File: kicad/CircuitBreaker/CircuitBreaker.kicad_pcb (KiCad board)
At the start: 2 copper layers, 71.6 x 27.5 mm, 59 parts, among them J1 PH2.54, J4 PH2.54, J5 downlink, J6 uplink, J7 PWN-In-5v, SW1 usbIAP, T1 CT104D, T2 CT104D, T3 CT104D, T4 CT104D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

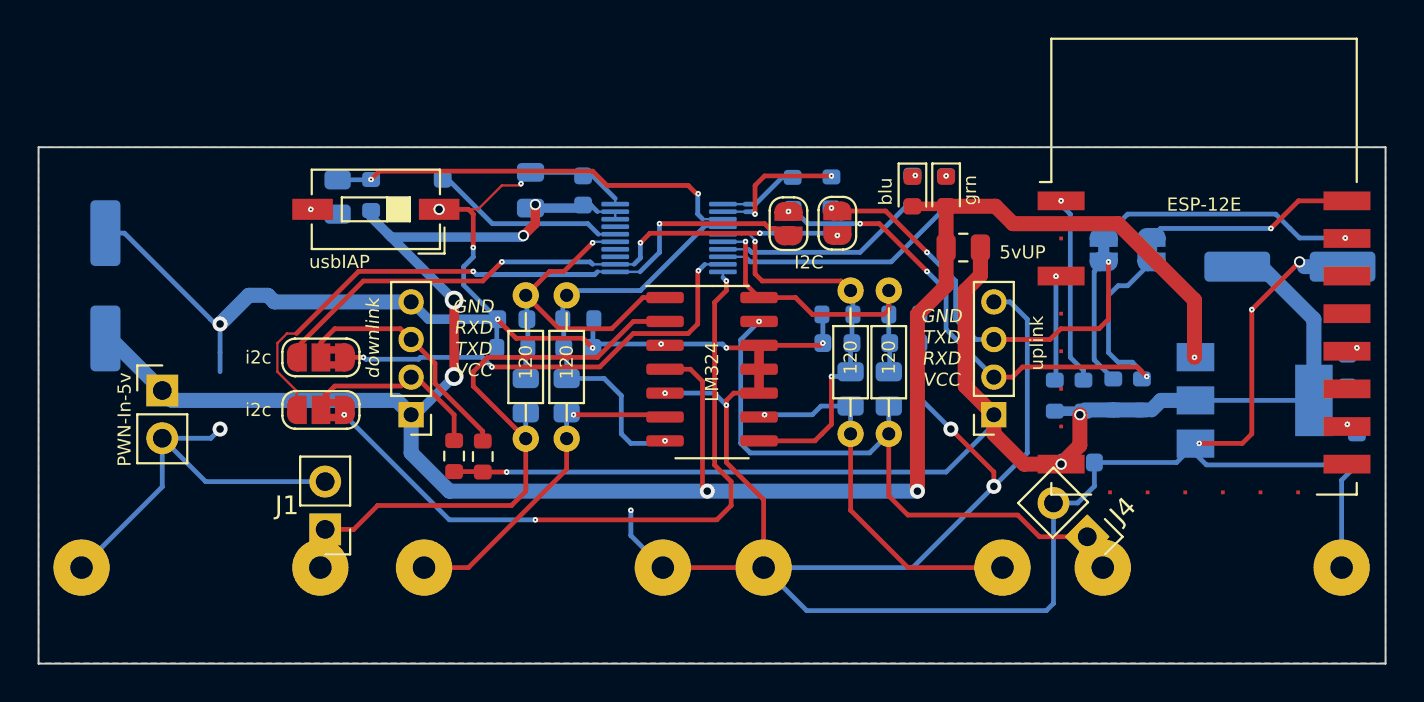
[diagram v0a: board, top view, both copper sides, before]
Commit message: corrected stc tssop20
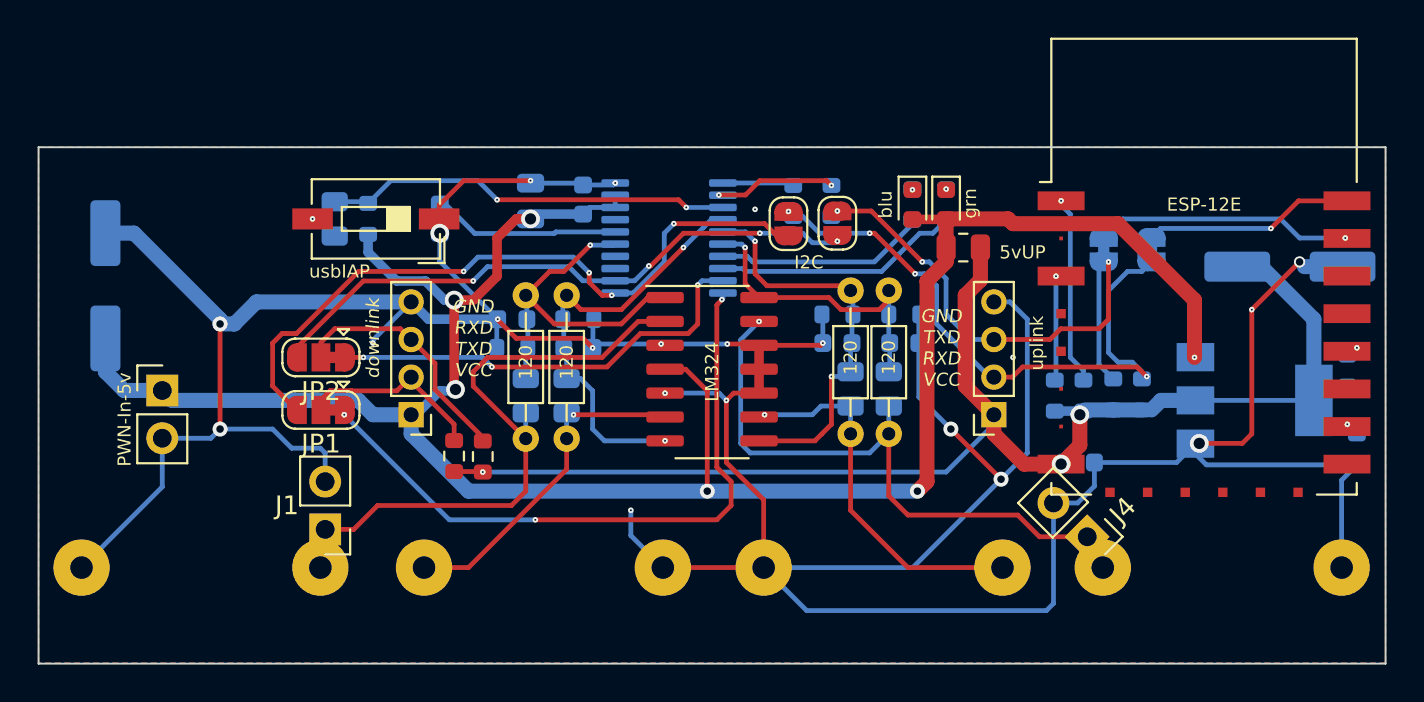
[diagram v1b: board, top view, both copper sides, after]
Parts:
- JP1, JP2: footprint Jumper:SolderJumper-3_P1.3mm_Bridged2Bar12_RoundedPad1.0x1.5mm_NumberLabels -> Jumper:SolderJumper-3_P1.3mm_Bridged12_RoundedPad1.0x1.5mm
- U2: footprint Package_SO:TSSOP-20_4.4x5mm_P0.4mm -> Package_SO:TSSOP-20_4.4x6.5mm_P0.65mm
- moved C5 1.33 mm to (72.1, 57.1)
- moved R15 1.28 mm to (68.3, 57.1)
- moved R16 1.18 mm to (66.5, 57.1)
- moved R27 0.73 mm to (97.3, 56.4)
- moved D1 0.70 mm to (99.1, 56.4)
- moved R26 0.70 mm to (99.1, 56.4)
- moved D2 0.69 mm to (97.3, 56.4)
- moved C7 0.57 mm to (77.0, 56.2)
- moved SW1 0.51 mm to (68.7, 57.1)
- moved C6 0.48 mm to (79.8, 56.1)
- moved R19 0.45 mm to (93.0, 56.2)
- moved R18 0.43 mm to (90.9, 56.2)
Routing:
- net SDA: track 40.5 -> 37.8 mm, vias 2 -> 4
- net +5V: track 120.0 -> 117.7 mm, vias 10 -> 9
- net DTXD: track 36.3 -> 34.9 mm
- net /P3.1: track 7.74 -> 6.41 mm
- net /P3.0: track 4.30 -> 3.41 mm
- net DRXD: track 24.3 -> 23.4 mm
- net ADC3: track 17.3 -> 16.5 mm
- net ADC1: track 22.3 -> 23.0 mm, vias 1 -> 2
- net Net-(R15-Pad2): track 22.4 -> 21.8 mm
- net GND: track 216.7 -> 217.3 mm, vias 18 -> 21

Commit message: cm104 add jack
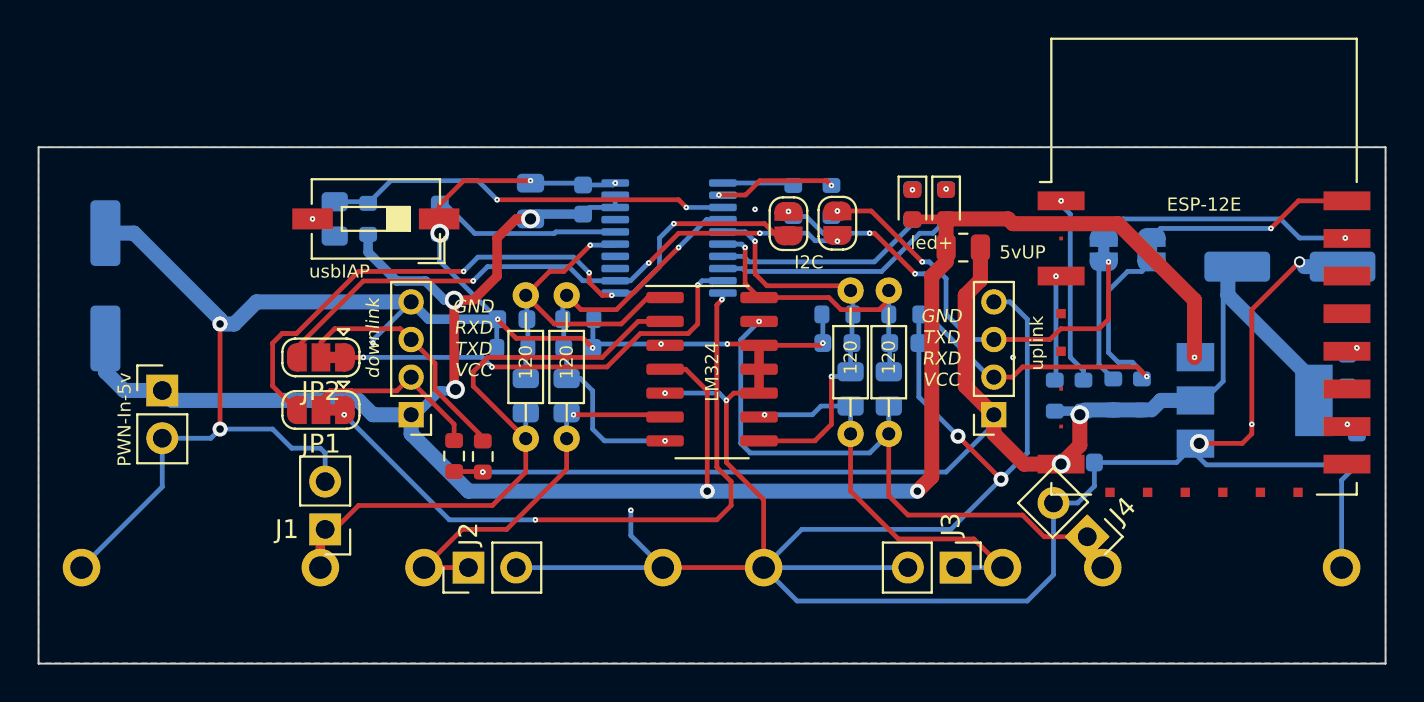
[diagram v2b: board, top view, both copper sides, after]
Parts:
- added J2: PH2.54, Connector_PinHeader_2.54mm:PinHeader_1x02_P2.54mm_Vertical, F.Cu at (73.7, 75.7)
- added J3: PH2.54, Connector_PinHeader_2.54mm:PinHeader_1x02_P2.54mm_Vertical, F.Cu at (99.6, 75.7)
- D1: value grn -> led+
- D2: value blu -> led
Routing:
- net GND: track 217.3 -> 231.7 mm
- net Net-(J2-Pad1): track 17.7 -> 20.0 mm
- net Net-(J3-Pad1): track 19.6 -> 21.5 mm
- net +3V3: track 74.3 -> 76.0 mm
- net Net-(J1-Pad1): track 31.7 -> 33.2 mm
